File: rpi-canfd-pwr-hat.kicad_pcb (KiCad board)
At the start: 4 copper layers, 80 parts, among them J1 Conn_01x02, J2 Conn_01x04_Pin, J3 Raspberry_Pi, J4 Conn_01x02, J5 Conn_01x02, U1 XC6206P332MR, U10 SN74LV1T125DBV, U11 SN74LV1T125DBV, U12 SN74LV1T125DBV, U13 SN74LV1T125DBV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

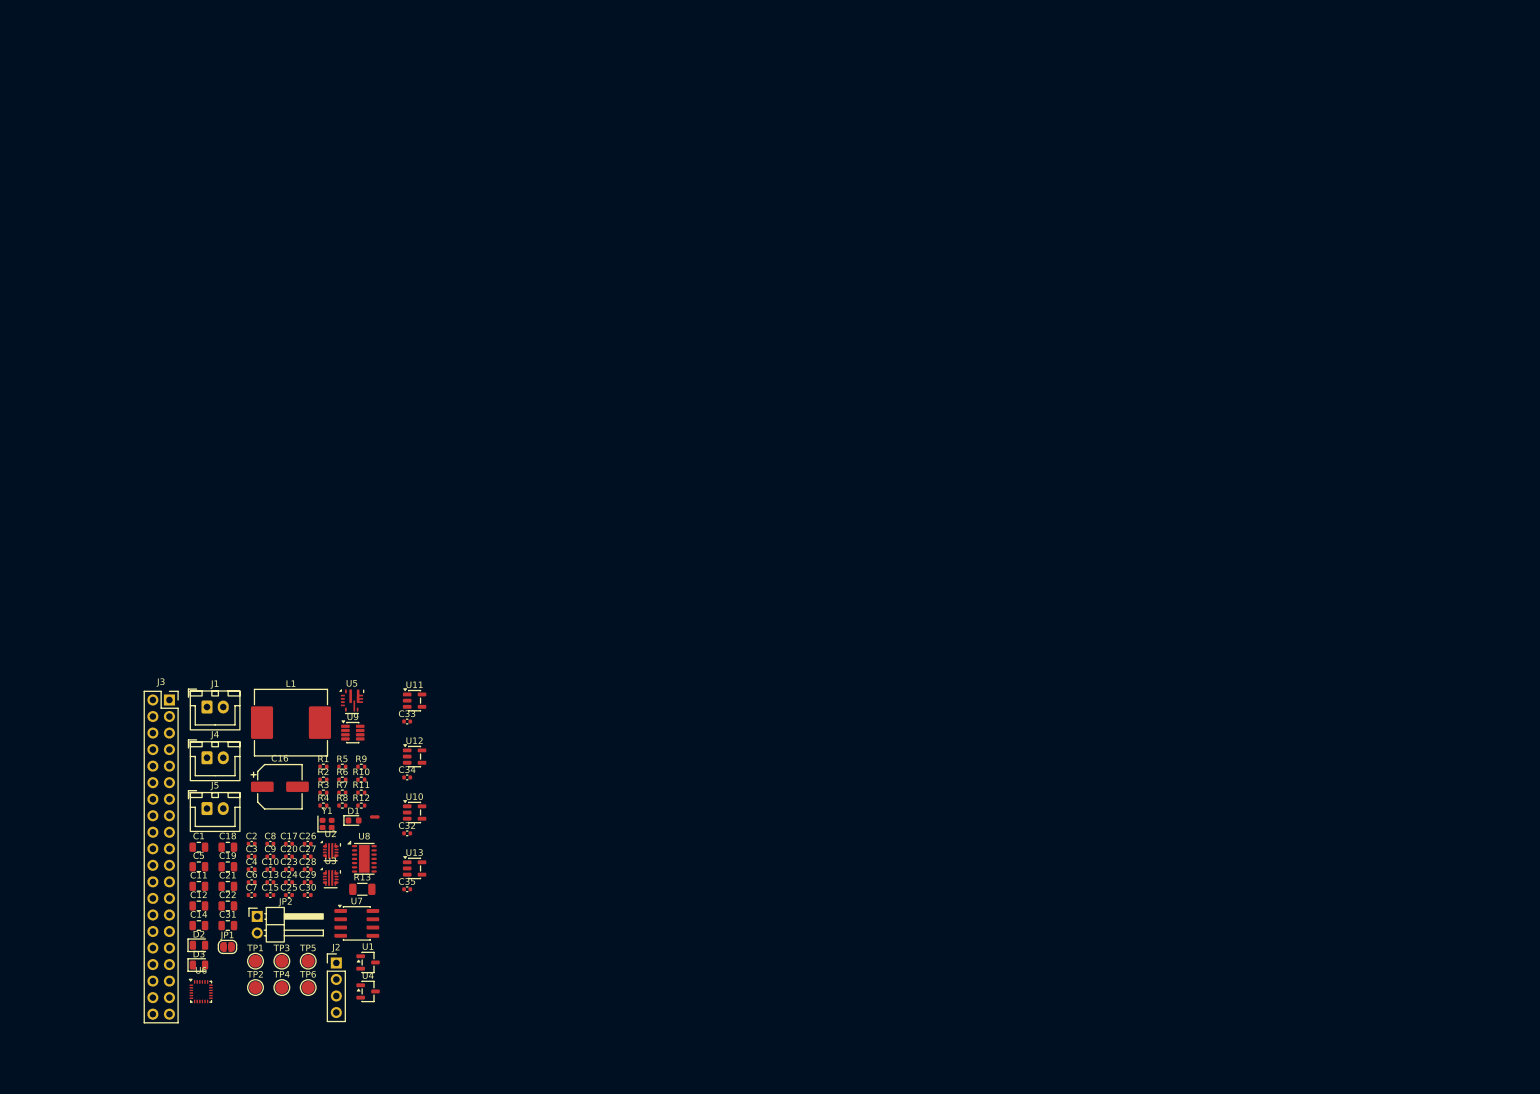
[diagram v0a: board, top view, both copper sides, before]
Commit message: pcb: initial sectionning
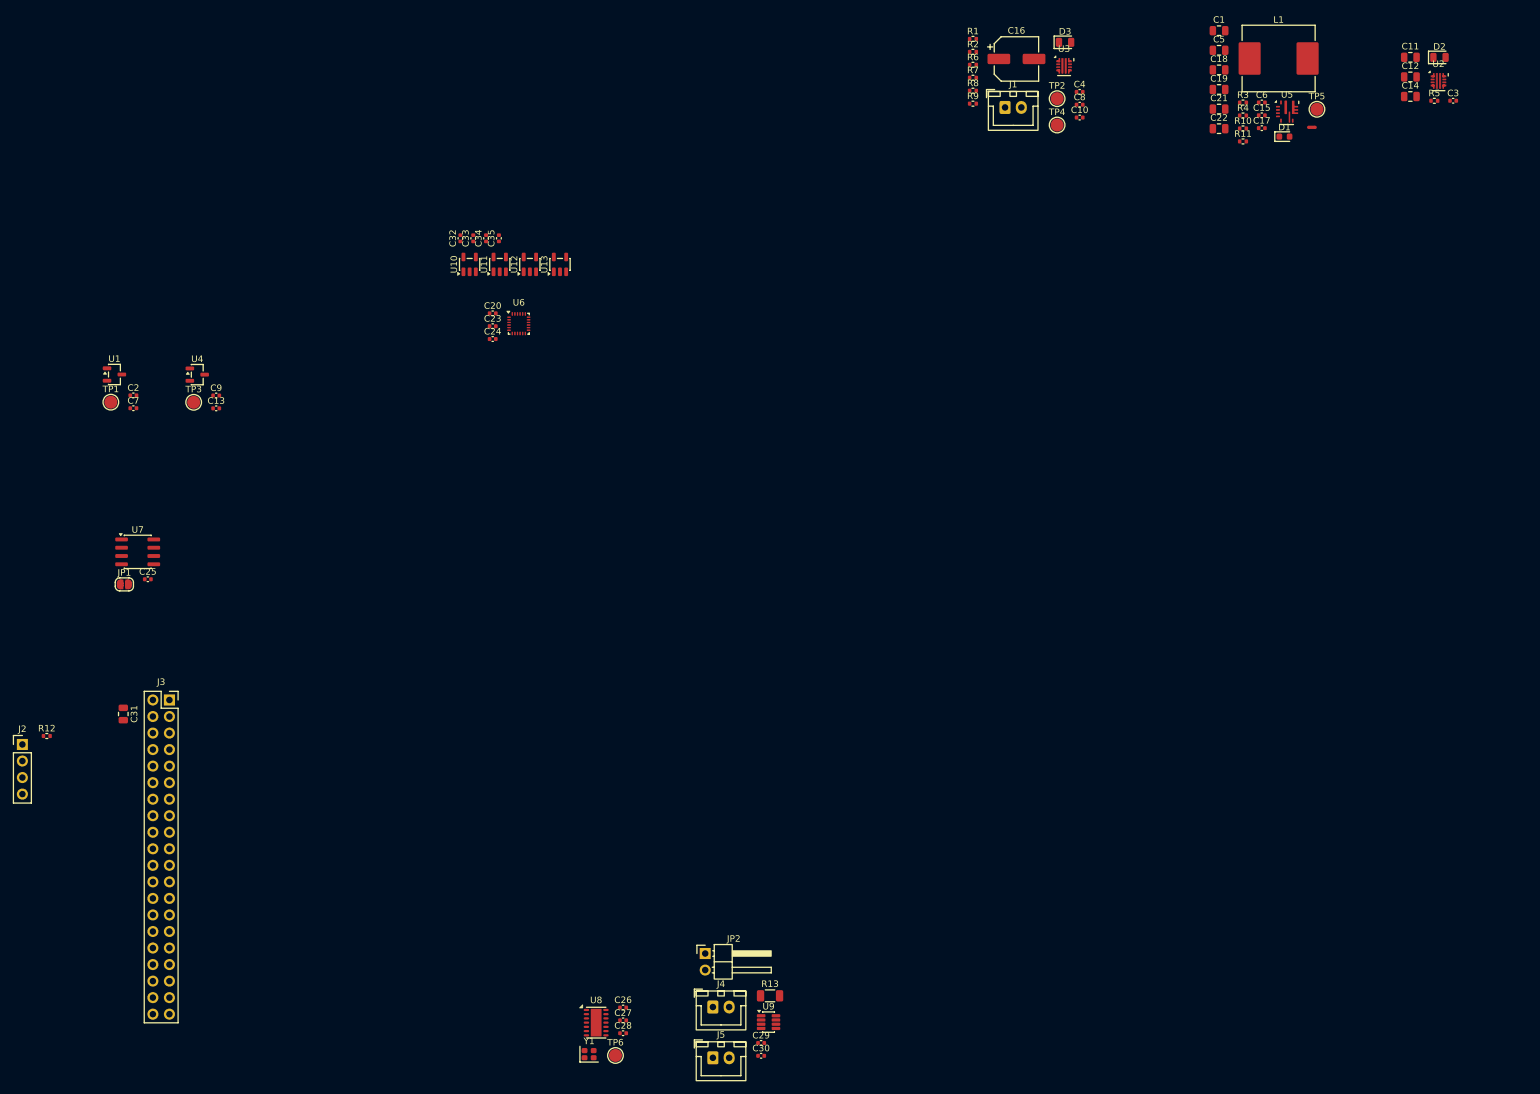
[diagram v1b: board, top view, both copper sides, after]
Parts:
- moved D2 234.3 mm to (237.4, 34.3)
- moved C11 225.5 mm to (232.9, 34.3)
- moved C12 225.5 mm to (232.9, 37.3)
- moved C14 225.5 mm to (232.9, 40.4)
- moved C3 218.0 mm to (239.5, 41.0)
- moved U2 207.2 mm to (237.3, 38.0)
- moved TP5 202.8 mm to (218.6, 42.3)
- moved C1 200.7 mm to (203.6, 30.2)
- moved C5 200.7 mm to (203.6, 33.2)
- moved R5 196.5 mm to (236.6, 41.0)
- moved C6 196.0 mm to (210.1, 41.3)
- moved D3 194.4 mm to (179.9, 32.0)
- moved C15 193.8 mm to (210.1, 43.2)
- moved C18 193.5 mm to (203.6, 36.3)
- moved C21 193.5 mm to (203.6, 42.3)
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
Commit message: pcb: add hat outline
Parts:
- added FID1: Fiducial, Fiducial:Fiducial_1mm_Mask2mm, F.Cu at (111.7, 116.8)
- added FID2: Fiducial, Fiducial:Fiducial_1mm_Mask2mm, F.Cu at (111.7, 120.3)
- added FID3: Fiducial, Fiducial:Fiducial_1mm_Mask2mm, F.Cu at (111.7, 123.9)
- added H1: MountingHole_Pad, MountingHole:MountingHole_2.7mm_M2.5_Pad_Via, F.Cu at (153.5, 73.5)
- added H2: MountingHole_Pad, MountingHole:MountingHole_2.7mm_M2.5_Pad_Via, F.Cu at (211.5, 73.5)
- added H3: MountingHole_Pad, MountingHole:MountingHole_2.7mm_M2.5_Pad_Via, F.Cu at (211.5, 122.5)
- added H4: MountingHole_Pad, MountingHole:MountingHole_2.7mm_M2.5_Pad_Via, F.Cu at (153.5, 122.5)
- added H5: MountingHole, MountingHole:ToolingHole_1.152mm, F.Cu at (111.2, 126.9)
- added H6: MountingHole, MountingHole:ToolingHole_1.152mm, F.Cu at (111.2, 129.3)
- added H7: MountingHole, MountingHole:ToolingHole_1.152mm, F.Cu at (111.2, 131.8)
- J3: moved to B.Cu
- moved J3 129.8 mm to (158.4, 74.8), turned to -90 degrees
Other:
- board outline added: 65 x 56 mm

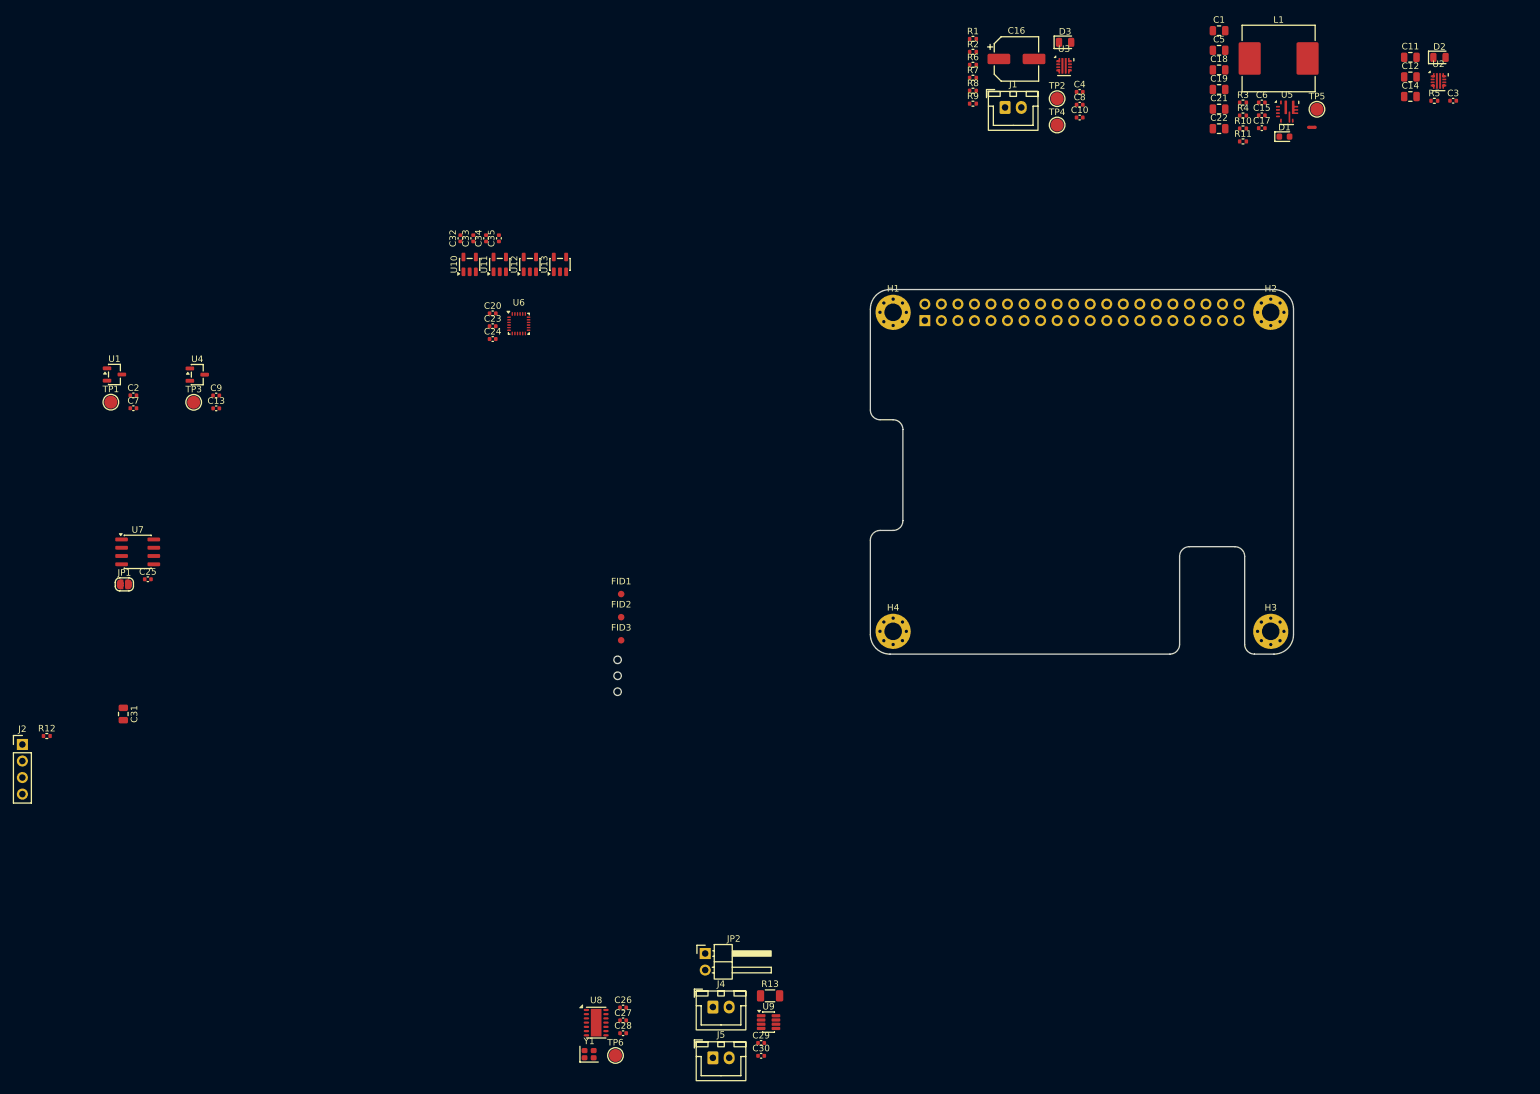
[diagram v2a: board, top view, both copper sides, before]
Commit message: pcb: add can layout
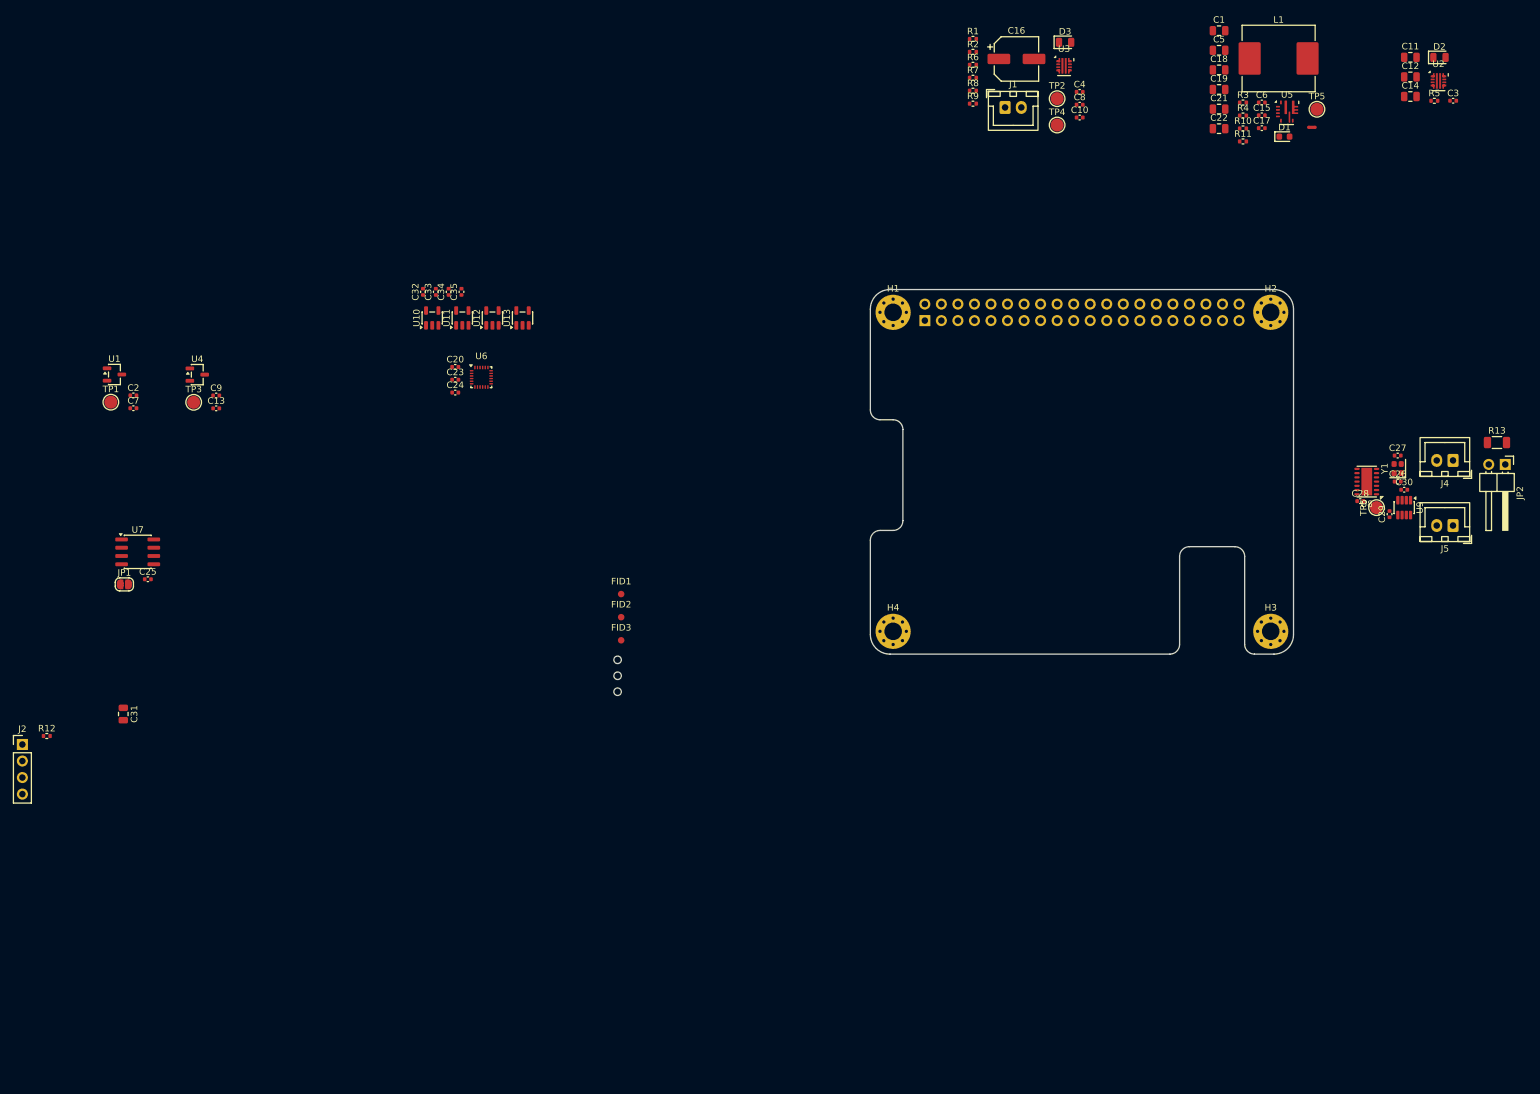
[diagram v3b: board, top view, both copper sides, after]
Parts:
- moved Y1 153.4 mm to (231.0, 97.5), turned to 90 degrees
- moved C27 147.3 mm to (231.0, 95.5)
- moved U8 144.6 mm to (226.2, 99.5), turned to 180 degrees
- moved TP6 144.0 mm to (227.8, 103.5), turned to 90 degrees
- moved JP2 144.0 mm to (247.5, 96.9), turned to -90 degrees
- moved C26 143.8 mm to (231.0, 99.5)
- moved J4 141.3 mm to (239.5, 96.2), turned to 180 degrees
- moved R13 140.3 mm to (246.2, 93.5)
- moved J5 140.0 mm to (239.5, 106.2), turned to 180 degrees
- moved C28 139.6 mm to (225.2, 102.5)
- moved C30 131.6 mm to (232.0, 100.8)
- moved C29 126.2 mm to (229.8, 104.5), turned to 90 degrees
- moved U9 125.6 mm to (232.0, 103.5), turned to -90 degrees
- moved C20 10.0 mm to (86.2, 81.9)
- moved C23 10.0 mm to (86.2, 83.9)
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
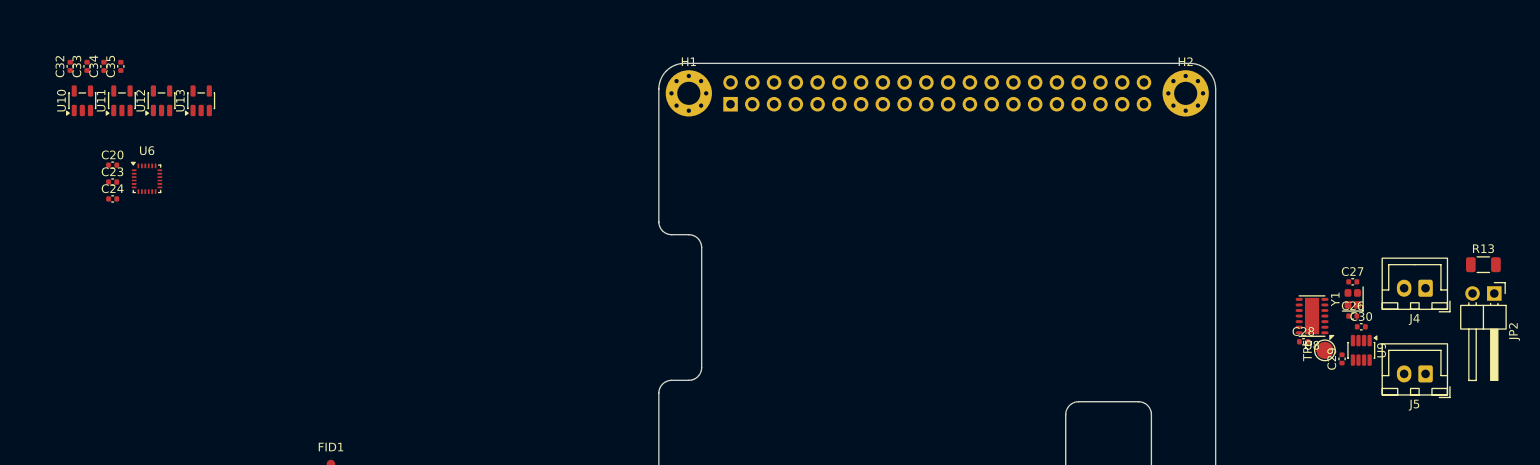
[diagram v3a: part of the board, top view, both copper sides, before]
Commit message: pcb: add imu layout
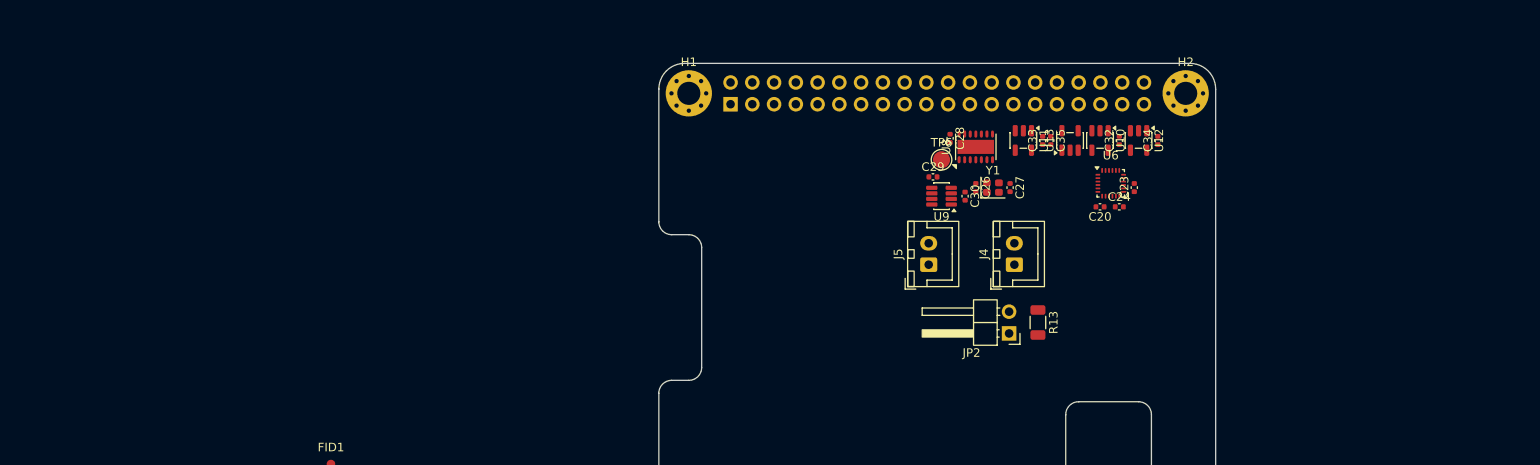
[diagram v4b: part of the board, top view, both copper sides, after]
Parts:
- moved C34 123.3 mm to (208.2, 79.0)
- moved C32 122.8 mm to (203.8, 79.0)
- moved C23 119.3 mm to (205.5, 84.5), turned to 90 degrees
- moved U10 118.9 mm to (201.5, 79.0), turned to -90 degrees
- moved C24 117.5 mm to (203.8, 86.8)
- moved C20 115.4 mm to (201.5, 86.8), turned to 180 degrees
- moved U12 114.1 mm to (206.0, 79.0), turned to -90 degrees
- moved U6 112.5 mm to (202.8, 84.0)
- moved C33 111.9 mm to (194.8, 79.0)
- moved C35 108.9 mm to (195.8, 79.0), turned to -90 degrees
- moved U11 105.3 mm to (192.6, 79.0), turned to -90 degrees
- moved U13 101.5 mm to (198.0, 79.0)
- moved J5 59.4 mm to (181.5, 93.5), turned to 90 degrees
- moved JP2 56.8 mm to (190.9, 101.5), turned to 180 degrees
- moved R13 52.4 mm to (194.2, 100.2), turned to -90 degrees
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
